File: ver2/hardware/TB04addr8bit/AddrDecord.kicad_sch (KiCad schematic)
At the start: 6 parts, among them U1 74AHC04, U39 74LS08, U40 74LS08

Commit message: ver2: ゲートICをgatesシートへ集約しアノテーションを掛け直し
- 分散していた8パッケージ(U1/U2/U5/U25/U35/U36/U37/U51)をgatesシートへ集約
- シートをまたぐ11本をグローバルラベル化(~P4/~P5/~OUT_SEL/~CS_RAM/
  ~OE_ROM/CLK_C/CLK_Z/PC_CNT_EN/~PC_PE/~Ena_RS01/~Enb_RS01)
- U40のP2入力がROM_SELに吸着していたのを修正(RAM_SELが逆条件だった)
- !P5の重複インバータを解消、未使用ゲート入力7本をGNDへ
- ALU入力MUXをinPut→PC、PCカウンタをaddrMUX→PCへ移動
- 全体を再アノテーション(シート順採番)。旧→新の対応は電気的変化なしを確認

Co-Authored-By: Claude Opus 5 <noreply@anthropic.com>
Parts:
- removed C57: 0.1u, symbol Device:C
- removed U1: 74AHC04, symbol 74xx:74AHC04
- renumbered C58 to C1301, C59 to C1302, U39 to U1301, U40 to U1302
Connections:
- net ~{OUT_SEL}: now reaches U1302.13
- net ~{P5}: now reaches U1302.10
- net ~{P4}: now reaches U1302.5
- net OUT_SEL renamed P6
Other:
- moved on the sheet: U1302B, U1302C, U1302D, U1302E

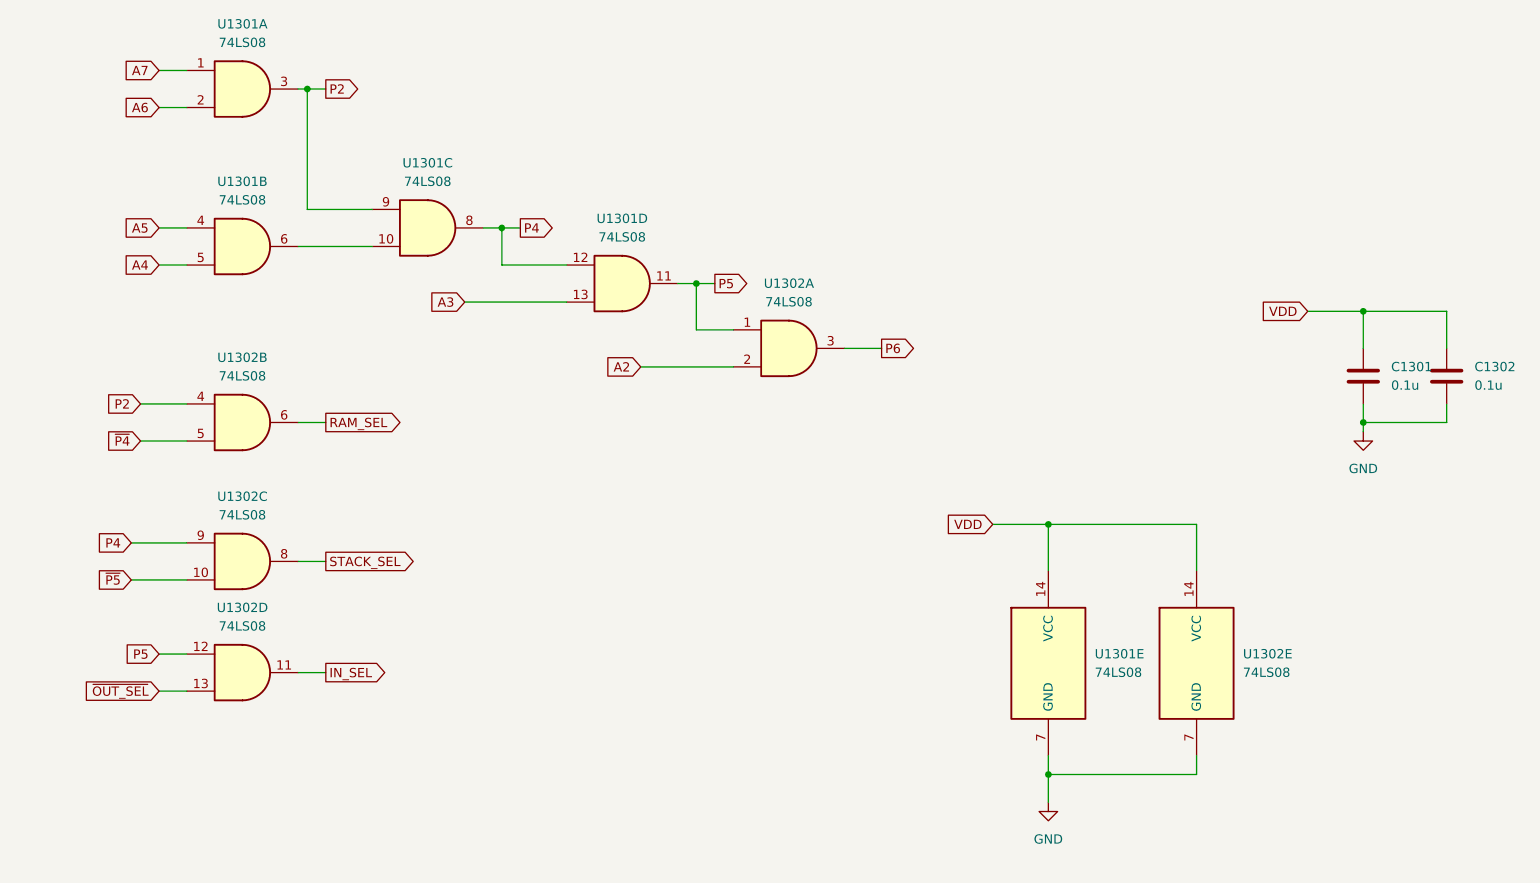
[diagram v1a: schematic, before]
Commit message: ver2: 掃除とタイミング是正(ROMのEXEゲート・フラグクロックをFCH1へ)
- 消費先ゼロだったU1302(RAM_SEL/STACK_SEL/IN_SEL/P6)を削除し空きゲート入力をGNDへ
- /OE_ROMの条件を生の~WRから~WR_EXE(=!(WR&EXE))へ変更
  書込命令の次のフェッチでROMが閉じる問題を解消
- フラグDFFのクロックゲートをEXEからFCH1へ(CLK_C=FCH1&C_WE)
  INのZが間に合わない件と、Cin=C_prevの帰還でADD/SUBの結果が壊れる件を解消
- いずれもネットリストで接続変化を照合済み。ERCはエラー98(全てwire_dangling)・警告0

Co-Authored-By: Claude Opus 5 <noreply@anthropic.com>
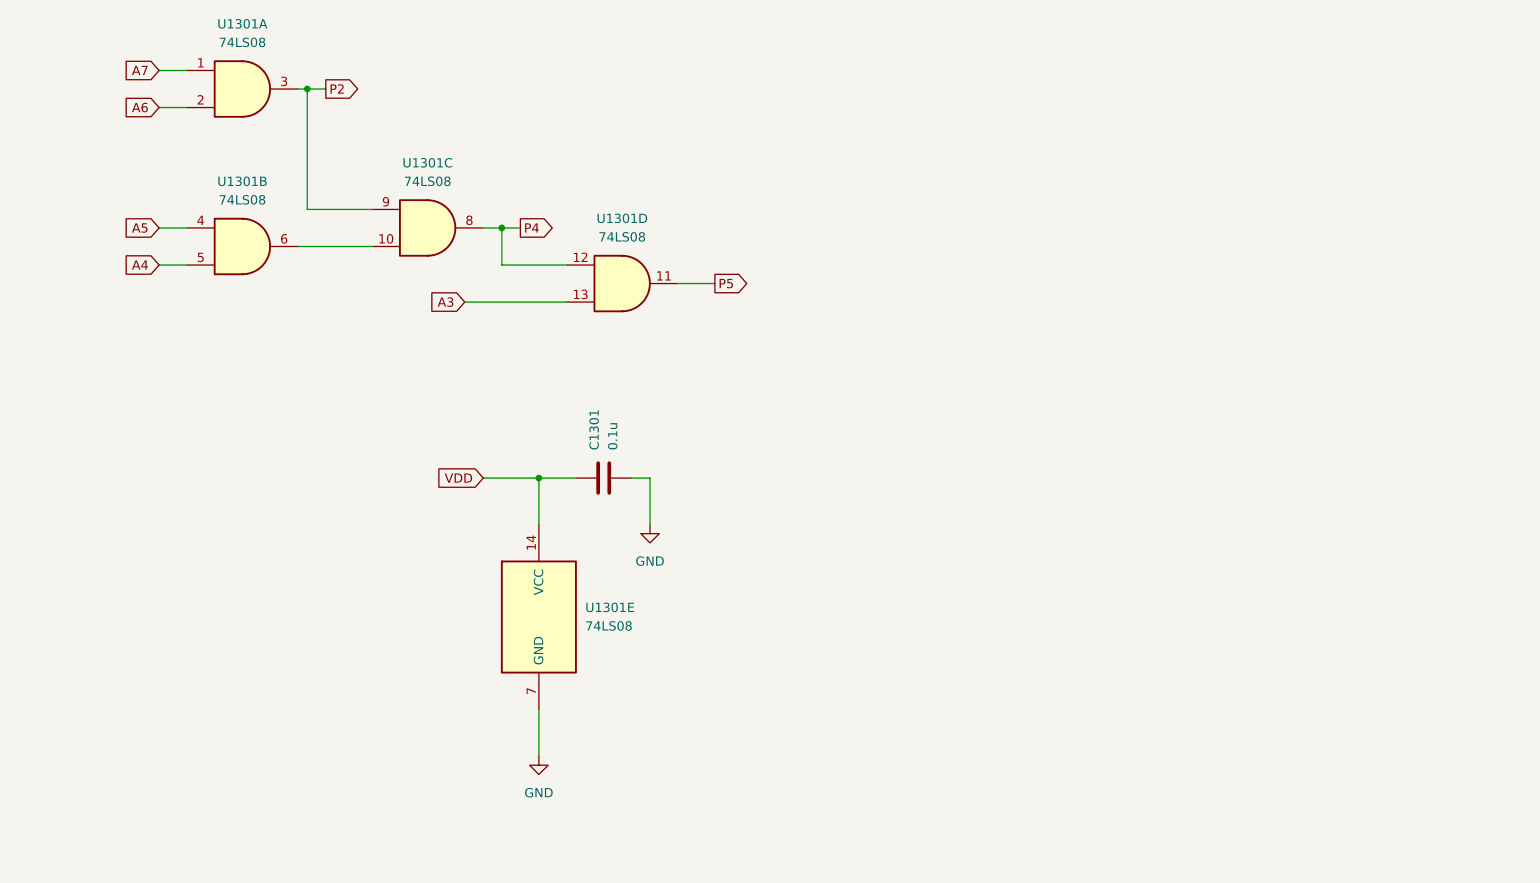
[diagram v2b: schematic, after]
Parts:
- removed C1302: 0.1u, symbol Device:C
- removed U1302: 74LS08, symbol 74xx:74LS08
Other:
- moved on the sheet: U1301E
